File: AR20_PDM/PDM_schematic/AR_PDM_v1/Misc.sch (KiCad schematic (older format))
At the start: 93 parts

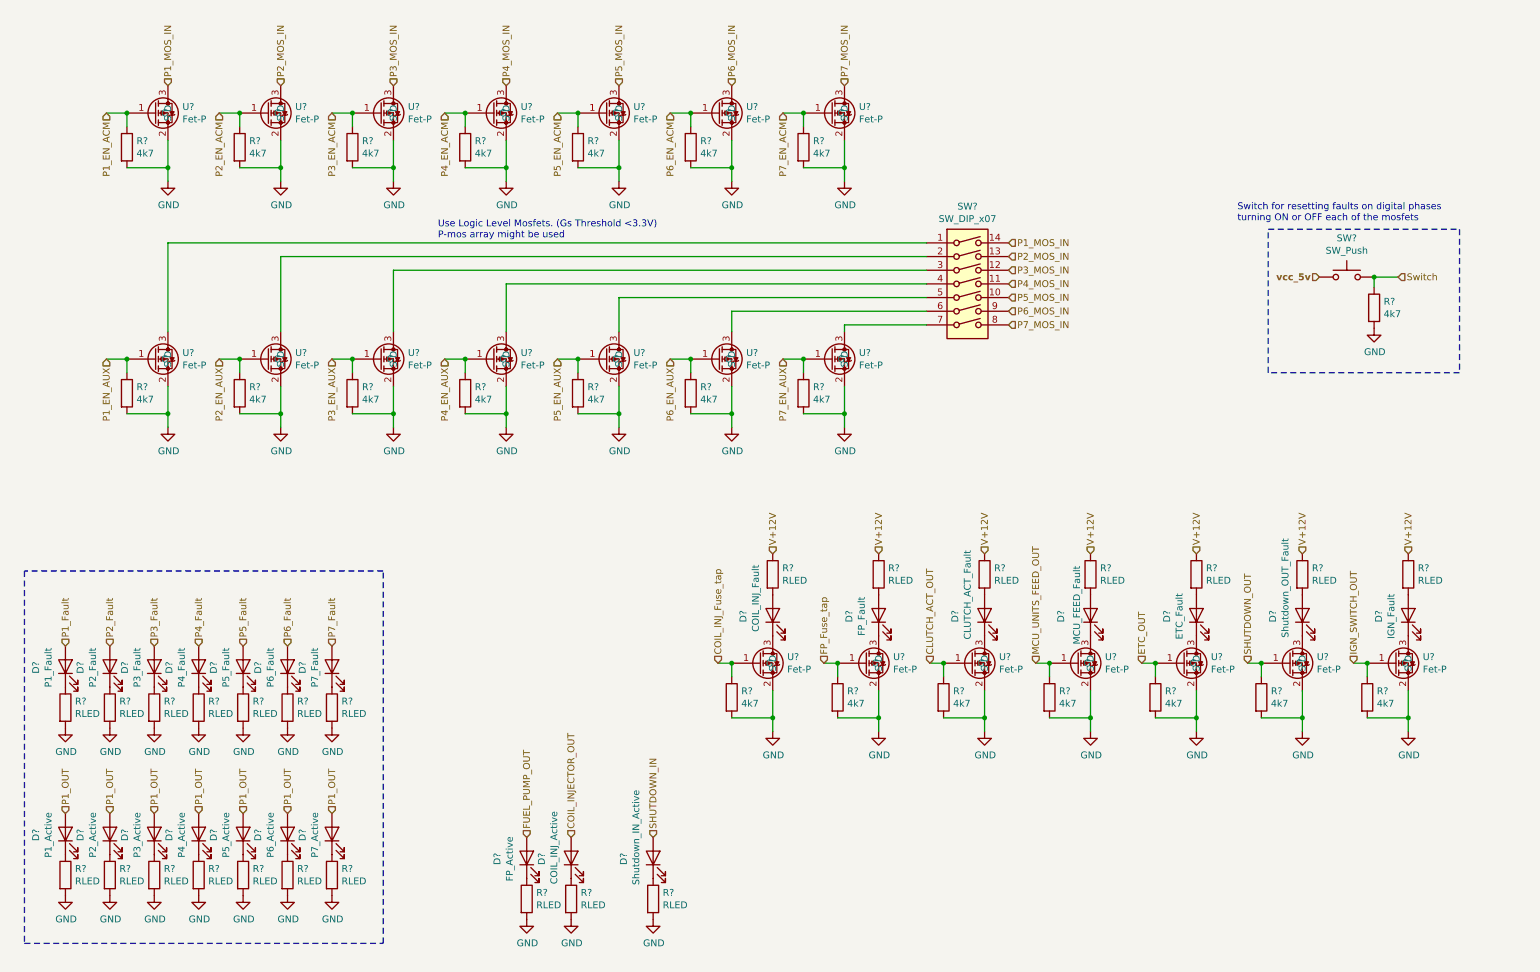
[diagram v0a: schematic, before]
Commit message: Added LEDs and switches.
- Added all status leds
- Added all switches
- ! Connections are work in progress, not everything is correct
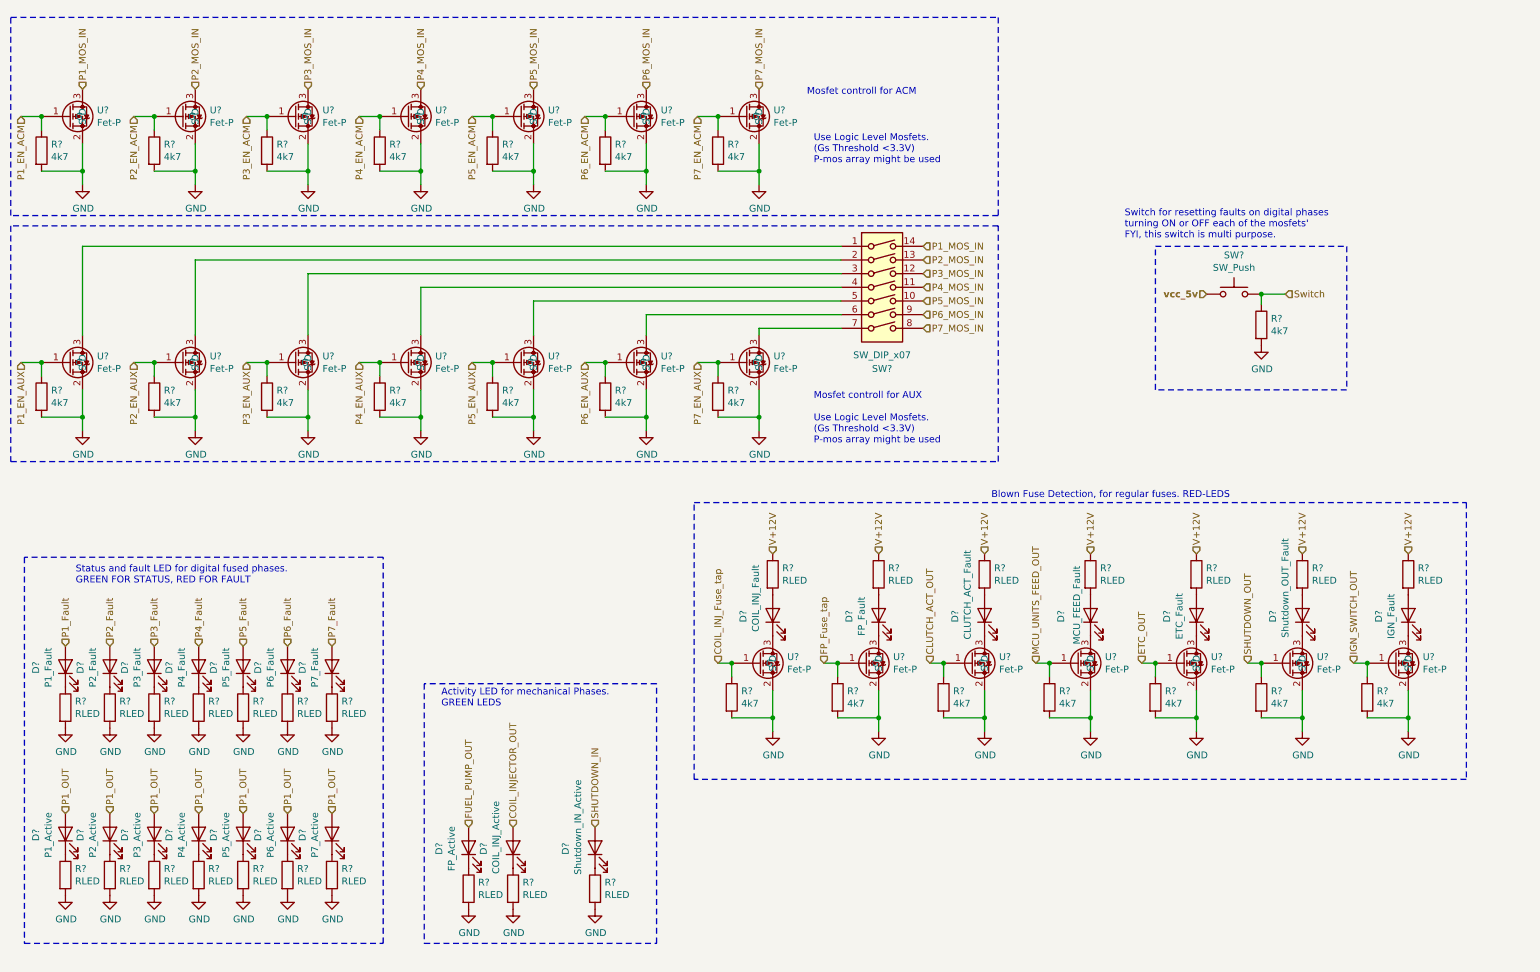
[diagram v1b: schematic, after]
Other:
- note added: "Activity LED for mechanical Phases. \nGREEN LEDS"
- note added: "Blown Fuse Detection, for regular fuses. RED-LEDS"
- note added: "Mosfet controll for ACM"
- note added: "Mosfet controll for AUX"
- note added: "Status and fault LED for digital fused phases.\nGREEN FOR STATUS, RED FOR FAULT"
- note added: "Switch for resetting faults on digital phases\nturning ON or OFF each of the mosfets'\nFYI, this switch is multi purpose."
- note added: "Use Logic Level Mosfets. \n(Gs Threshold <3.3V)\nP-mos array might be used"
- note removed: "Switch for resetting faults on digital phases\nturning ON or OFF each of the mosfets"
- note removed: "Use Logic Level Mosfets. (Gs Threshold <3.3V)\nP-mos array might be used"
- moved on the sheet: D?, R?, SW?, U?

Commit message: Fixed wrong value components and ports, wiring, see discription
- Fixed supply cappacitor value 220 nf to 100nf
- Fixed IN cappacitor value 220 nf to 150 nf
- Fixed out cappacitor value, 220nf to 10 nf
- Made a mux for mosfet sense
- Found a I/O port expander
- Added some and removed some leds
- Fixed all labels, and wired everything up, besides the connectors
- Still missing connector and acm connector pinout.
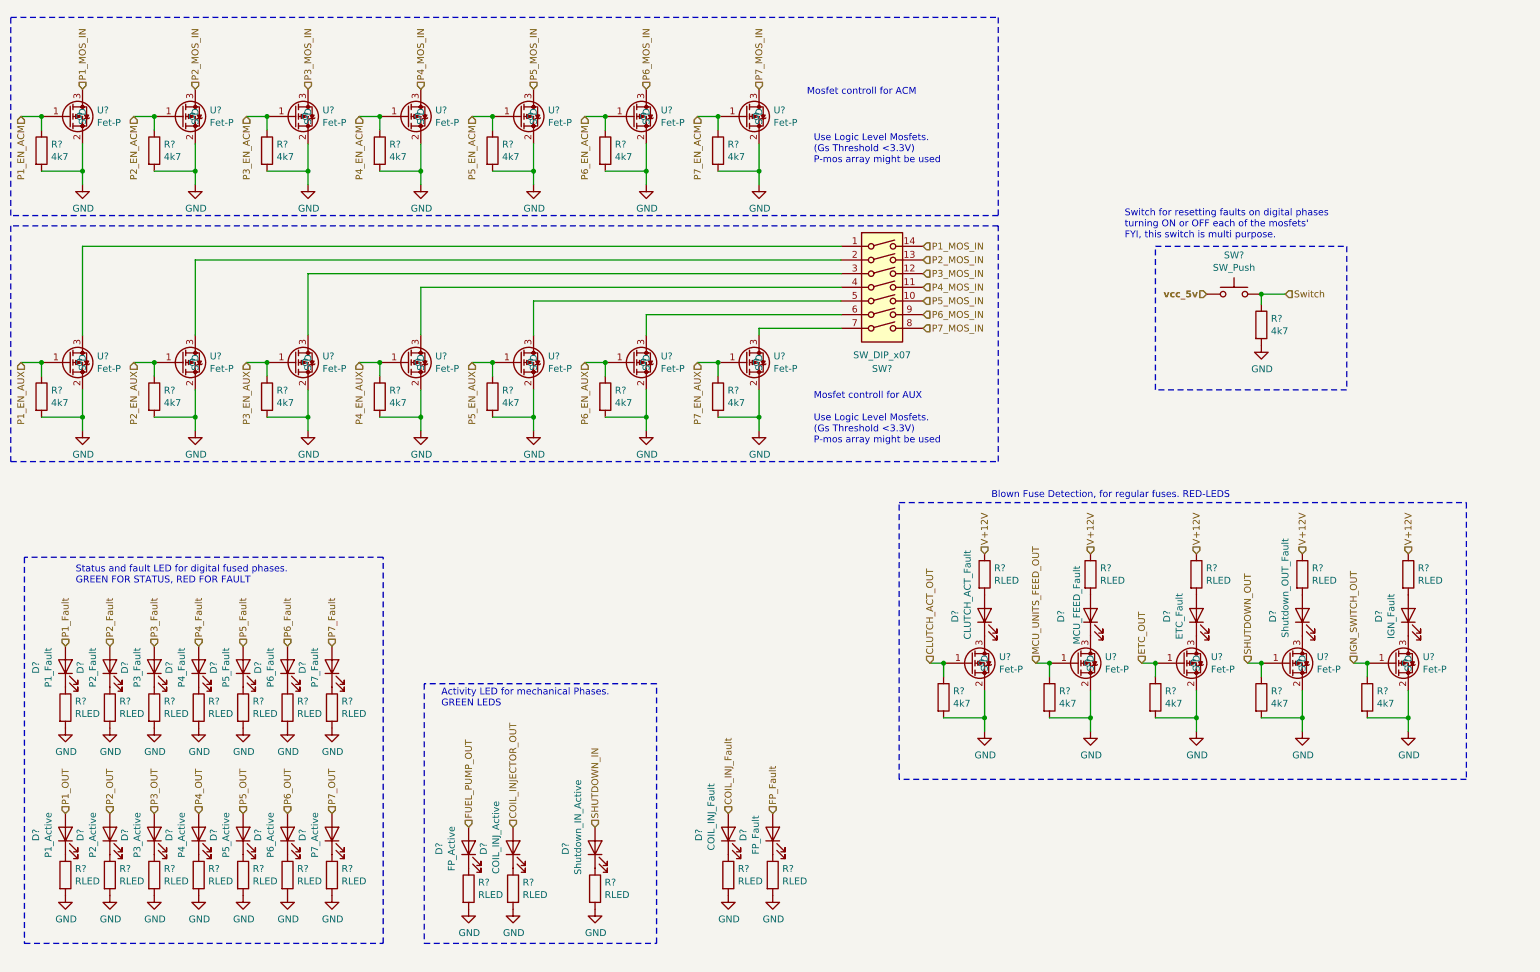
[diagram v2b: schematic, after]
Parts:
- removed R? (x2): RLED, symbol AR20_PDM_v1-rescue:R-Device
- removed R? (x2): 4k7, symbol AR20_PDM_v1-rescue:R-Device
- removed U? (x2): Fet-P, symbol AR20_PDM_v1-rescue:GenericFet-P
- added R? (x2): RLED, symbol AR20_PDM_v1-rescue:R-Device
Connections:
- net GND: now also R?.2, R?.2
- net P1_OUT: no longer D?.2 (A), D?.2 (A), D?.2 (A), D?.2 (A), D?.2 (A), D?.2 (A)
- net FP_Fault: now reaches D?.2 (A)
- net at D?.1 (K): now also R?.1 (x2)
- net COIL_INJ_Fault: now reaches D?.2 (A)
- new net P2_OUT: D?.2 (A)
- new net P3_OUT: D?.2 (A)
- new net P4_OUT: D?.2 (A)
- new net P5_OUT: D?.2 (A)
- new net P6_OUT: D?.2 (A)
- new net P7_OUT: D?.2 (A)
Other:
- moved on the sheet: D?

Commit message: Fixed issues, controlled components, BOM, see discription
- added acm symbol
- fixed wrongly faced P-mosfets
- I/O expander now sinks led instead of source
- Bill of material mostly done
- Correct address for INA233 chips.
- Now 4 diodes serves as flyback for all mosfets
- Corrected naming scheme for compmonents (everything is not fixed yet)
- Fixed some labels
- altso some minor changes
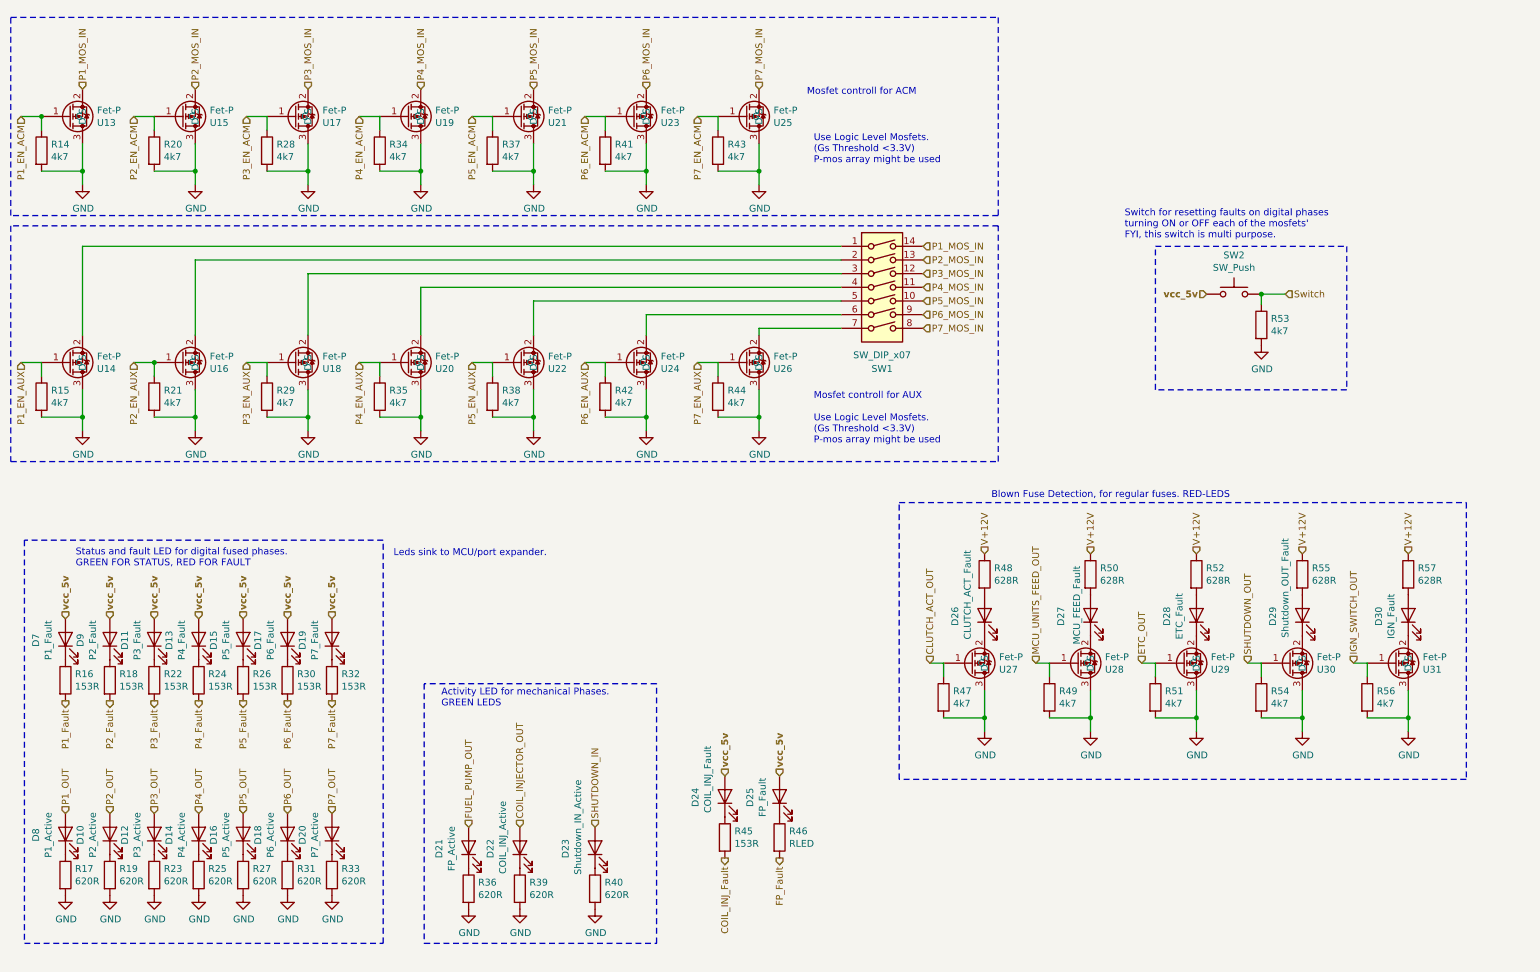
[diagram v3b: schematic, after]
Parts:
- removed U? (x18): Fet-P, symbol AR20_PDM_v1-rescue:GenericFet-P
- added U14, U15, U16, U17, U18, U19, U20, U21, U22, U23, U24, U25, U26, U27, U28, U29, U30, U31: Fet-P, symbol AR20_PDM_v1-rescue:GenericFet-P
- R16, R18, R22, R24, R26, R30, R32, R45: renamed from R?; value RLED -> 153R
- R17, R19, R23, R25, R27, R31, R33, R36, R39, R40: renamed from R?; value RLED -> 620R
- R48, R50, R52, R55, R57: renamed from R?; value RLED -> 628R
- gave numbers to parts that had none: 48
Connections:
- net CLUTCH_ACT_OUT: now also U27.1 (G)
- net COIL_INJ_Fault: now also R45.2; no longer D24.2 (A)
- net ETC_OUT: now also U29.1 (G)
- net FP_Fault: now also R46.2; no longer D25.2 (A)
- net GND: now also U13.3 (D), U14.3 (D), U15.3 (D), U16.3 (D), U17.3 (D), U18.3 (D), U19.3 (D), U20.3 (D), U21.3 (D), U22.3 (D), U23.3 (D), U24.3 (D), U25.3 (D), U26.3 (D), U27.3 (D), U28.3 (D), U29.3 (D), U30.3 (D), U31.3 (D); no longer R16.2, R18.2, R22.2, R24.2, R26.2, R30.2, R32.2, R45.2, R46.2, U13.2 (S)
- net IGN_SWITCH_OUT: now also U31.1 (G)
- net MCU_UNITS_FEED_OUT: now also U28.1 (G)
- net P1_EN_AUX: now also U14.1 (G)
- net P1_Fault: now also R16.2; no longer D7.2 (A)
- net P1_MOS_IN: now also U13.2 (S); no longer U13.3 (D)
- net P2_EN_ACM: now also U15.1 (G)
- net P2_EN_AUX: now also U16.1 (G)
- net P2_Fault: now also R18.2; no longer D9.2 (A)
- net P2_MOS_IN: now also U15.2 (S)
- net P3_EN_ACM: now also U17.1 (G)
- net P3_EN_AUX: now also U18.1 (G)
- net P3_Fault: now also R22.2; no longer D11.2 (A)
- net P3_MOS_IN: now also U17.2 (S)
- net P4_EN_ACM: now also U19.1 (G)
- net P4_EN_AUX: now also U20.1 (G)
- net P4_Fault: now also R24.2; no longer D13.2 (A)
- net P4_MOS_IN: now also U19.2 (S)
- net P5_EN_ACM: now also U21.1 (G)
- net P5_EN_AUX: now also U22.1 (G)
- net P5_Fault: now also R26.2; no longer D15.2 (A)
- net P5_MOS_IN: now also U21.2 (S)
- net P6_EN_ACM: now also U23.1 (G)
- net P6_EN_AUX: now also U24.1 (G)
- net P6_Fault: now also R30.2; no longer D17.2 (A)
- net P6_MOS_IN: now also U23.2 (S)
- net P7_EN_ACM: now also U25.1 (G)
- net P7_EN_AUX: now also U26.1 (G)
- net P7_Fault: now also R32.2; no longer D19.2 (A)
- net P7_MOS_IN: now also U25.2 (S)
- net SHUTDOWN_OUT: now also U30.1 (G)
- net vcc_5v: now also D11.2 (A), D13.2 (A), D15.2 (A), D17.2 (A), D19.2 (A), D24.2 (A), D25.2 (A), D7.2 (A), D9.2 (A)
- net at SW1.1: now also U14.2 (S)
- net at SW1.2: now also U16.2 (S)
- net at SW1.3: now also U18.2 (S)
- net at SW1.4: now also U20.2 (S)
- net at SW1.5: now also U22.2 (S)
- net at SW1.6: now also U24.2 (S)
- net at SW1.7: now also U26.2 (S)
- net at D30.1 (K): now also U31.2 (S)
- net at D29.1 (K): now also U30.2 (S)
- net at D28.1 (K): now also U29.2 (S)
- net at D27.1 (K): now also U28.2 (S)
- net at D26.1 (K): now also U27.2 (S)
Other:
- note added: "Leds sink to MCU/port expander."
- moved on the sheet: D11, D13, D15, D17, D19, D22, D24, D25, D7, D9, R16, R18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

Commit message: PCB design, and issue fixing, work in progress
- Error fixed: Mux mosfet resistor change to ground
- Open drain output added on phase 6, for engine blipping purpose
- Most of pcb symbols and footprints are finished, including main connector
- PCB is change from 1oz to 2oz copper layer, for easier routing.
- Basic Draft of pcb is done, for now.
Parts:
- D10, D11, D12, D13, D14, D15, D16, D17, D18, D19, D20, D21, D22, D23, D24, D25, D26, D27, D28, D29, D30, D7, D8, D9: footprint (none) -> LED_SMD:LED_1206_3216Metric
- R14, R15, R16, R17, R18, R19, R20, R21, R22, R23, R24, R25, R26, R27, R28, R29, R30, R31, R32, R33, R34, R35, R36, R37, R38, R39, R40, R41, R42, R43, R44, R45, R46, R47, R48, R49, R50, R51, R52, R53, R54, R55, R56, R57: footprint (none) -> Resistor_SMD:R_0603_1608Metric
- SW1: footprint (none) -> AR_PDM_v1:DIPSwitch
- SW2: footprint (none) -> Connector_JST:JST_EH_B2B-EH-A_1x02_P2.50mm_Vertical
- U13, U14, U15, U16, U17, U18, U19, U20, U21, U22, U23, U24, U25, U26, U27, U28, U29, U30, U31: footprint (none) -> Package_TO_SOT_SMD:SOT-23

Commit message: PCB Design, Work in progress
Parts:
- added D31: Shutdown_IN_Active, LED_SMD:LED_1206_3216Metric, symbol Device:LED
- added R59: 620R, Resistor_SMD:R_0603_1608Metric, symbol AR20_PDM_v1-rescue:R-Device
- D23: value Shutdown_IN_Active -> Shutdown_Circuit_Active
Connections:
- net GND: now also R59.2
- net SHUTDOWN_IN: now also D31.2 (A); no longer D23.2 (A)
- net P1_OUT renamed P1_Shunt
- net P2_OUT renamed P2_Shunt
- net P3_OUT renamed P3_Shunt
- net P4_OUT renamed P4_Shunt
- net P5_OUT renamed P5_Shunt
- net P6_OUT renamed P6_Shunt
- net P7_OUT renamed P7_Shunt
- new net: D31.1 (K), R59.1
- new net Shutdown_Led: D23.2 (A)
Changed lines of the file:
@@
 $Descr A4 11693 8268
 encoding utf-8
-Sheet 13 13
+Sheet 12 13
 Title ""
 Date ""
@@
 AR Path="/5DA89415/5E4973F5" Ref="D?"  Part="1"
 F 0 "D23" H 4793 6916 50  0000 C CNN
-F 1 "Shutdown_IN_Active" H 4950 6825 50  0000 C CNN
+F 1 "Shutdown_Circuit_Active" H 4950 6825 50  0000 C CNN
 F 2 "LED_SMD:LED_1206_3216Metric" H 4800 6700 50  0001 C CNN
 F 3 "~" H 4800 6700 50  0001 C CNN
@@
 	1    0    0    -1
 $EndComp
-Text HLabel 925  6450 1    50   Input ~ 0
-P1_OUT
 Text HLabel 1250 6450 1    50   Input ~ 0
-P2_OUT
+P2_Shunt
 Text HLabel 1575 6450 1    50   Input ~ 0
-P3_OUT
+P3_Shunt
 Text HLabel 1900 6450 1    50   Input ~ 0
-P4_OUT
+P4_Shunt
 Text HLabel 2225 6450 1    50   Input ~ 0
-P5_OUT
+P5_Shunt
 Text HLabel 2550 6450 1    50   Input ~ 0
-P6_OUT
+P6_Shunt
 Text HLabel 2875 6450 1    50   Input ~ 0
-P7_OUT
+P7_Shunt
 Text HLabel 4800 6550 1    50   Input ~ 0
-SHUTDOWN_IN
+Shutdown_Led
 Text HLabel 4250 6550 1    50   Input ~ 0
 COIL_INJECTOR_OUT
@@
 	1    0    0    1
 $EndComp
+$Comp
+L Device:LED D31
+U 1 1 5E39DADA
+P 5150 6700
+AR Path="/5E5484EE/5E39DADA" Ref="D31"  Part="1"
+AR Path="/5DA89415/5E39DADA" Ref="D?"  Part="1"
+F 0 "D31" H 5143 6916 50  0000 C CNN
+F 1 "Shutdown_IN_Active" H 5300 6825 50  0000 C CNN
+F 2 "LED_SMD:LED_1206_3216Metric" H 5150 6700 50  0001 C CNN
+F 3 "~" H 5150 6700 50  0001 C CNN
+	1    5150 6700
+	0    -1   -1   0
+$EndComp
+$Comp
+L AR20_PDM_v1-rescue:GND-power #PWR?
+U 1 1 5E39DAE0
+P 5150 7150
+AR Path="/5DA89415/5E39DAE0" Ref="#PWR?"  Part="1"
+AR Path="/5DEB10A1/5E39DAE0" Ref="#PWR?"  Part="1"
+AR Path="/5DEB20EA/5E39DAE0" Ref="#PWR?"  Part="1"
+AR Path="/5E0E4725/5E39DAE0" Ref="#PWR?"  Part="1"
+AR Path="/5E0E4A93/5E39DAE0" Ref="#PWR?"  Part="1"
+AR Path="/5E0E4EB5/5E39DAE0" Ref="#PWR?"  Part="1"
+AR Path="/5E0E5304/5E39DAE0" Ref="#PWR?"  Part="1"
+AR Path="/5E0E594B/5E39DAE0" Ref="#PWR?"  Part="1"
+AR Path="/5E0E607C/5E39DAE0" Ref="#PWR?"  Part="1"
+AR Path="/5E0FB5C8/5E39DAE0" Ref="#PWR?"  Part="1"
+AR Path="/5E0FBBBD/5E39DAE0" Ref="#PWR?"  Part="1"
+AR Path="/5E0FC3A2/5E39DAE0" Ref="#PWR?"  Part="1"
+AR Path="/5E0FCFDC/5E39DAE0" Ref="#PWR?"  Part="1"
+AR Path="/5E0FDCCC/5E39DAE0" Ref="#PWR?"  Part="1"
+AR Path="/5E10174B/5E39DAE0" Ref="#PWR?"  Part="1"
+AR Path="/5E5484EE/5E39DAE0" Ref="#PWR0133"  Part="1"
+F 0 "#PWR0133" H 5150 6900 50  0001 C CNN
+F 1 "GND" H 5155 6977 50  0000 C CNN
+F 2 "" H 5150 7150 50  0001 C CNN
+F 3 "" H 5150 7150 50  0001 C CNN
+	1    5150 7150
+	1    0    0    -1
+$EndComp
+$Comp
+L AR20_PDM_v1-rescue:R-Device R?
+U 1 1 5E39DAE6
+P 5150 7000
+AR Path="/5DA89415/5E39DAE6" Ref="R?"  Part="1"
+AR Path="/5DEB10A1/5E39DAE6" Ref="R?"  Part="1"
+AR Path="/5DEB20EA/5E39DAE6" Ref="R?"  Part="1"
+AR Path="/5E0E4725/5E39DAE6" Ref="R?"  Part="1"
+AR Path="/5E0E4A93/5E39DAE6" Ref="R?"  Part="1"
+AR Path="/5E0E4EB5/5E39DAE6" Ref="R?"  Part="1"
+AR Path="/5E0E5304/5E39DAE6" Ref="R?"  Part="1"
+AR Path="/5E0E594B/5E39DAE6" Ref="R?"  Part="1"
+AR Path="/5E0E607C/5E39DAE6" Ref="R?"  Part="1"
+AR Path="/5E0FB5C8/5E39DAE6" Ref="R?"  Part="1"
+AR Path="/5E0FBBBD/5E39DAE6" Ref="R?"  Part="1"
+AR Path="/5E0FC3A2/5E39DAE6" Ref="R?"  Part="1"
+AR Path="/5E0FCFDC/5E39DAE6" Ref="R?"  Part="1"
+AR Path="/5E0FDCCC/5E39DAE6" Ref="R?"  Part="1"
+AR Path="/5E10174B/5E39DAE6" Ref="R?"  Part="1"
+AR Path="/5E5484EE/5E39DAE6" Ref="R59"  Part="1"
+F 0 "R59" H 5220 7046 50  0000 L CNN
+F 1 "620R" H 5220 6955 50  0000 L CNN
+F 2 "Resistor_SMD:R_0603_1608Metric" V 5080 7000 50  0001 C CNN
+F 3 "~" H 5150 7000 50  0001 C CNN
+	1    5150 7000
+	1    0    0    -1
+$EndComp
+Text HLabel 5150 6550 1    50   Input ~ 0
+SHUTDOWN_IN
+Text HLabel 925  6450 1    50   Input ~ 0
+P1_Shunt
 $EndSCHEMATC
